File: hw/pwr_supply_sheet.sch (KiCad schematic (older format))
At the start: 11 parts

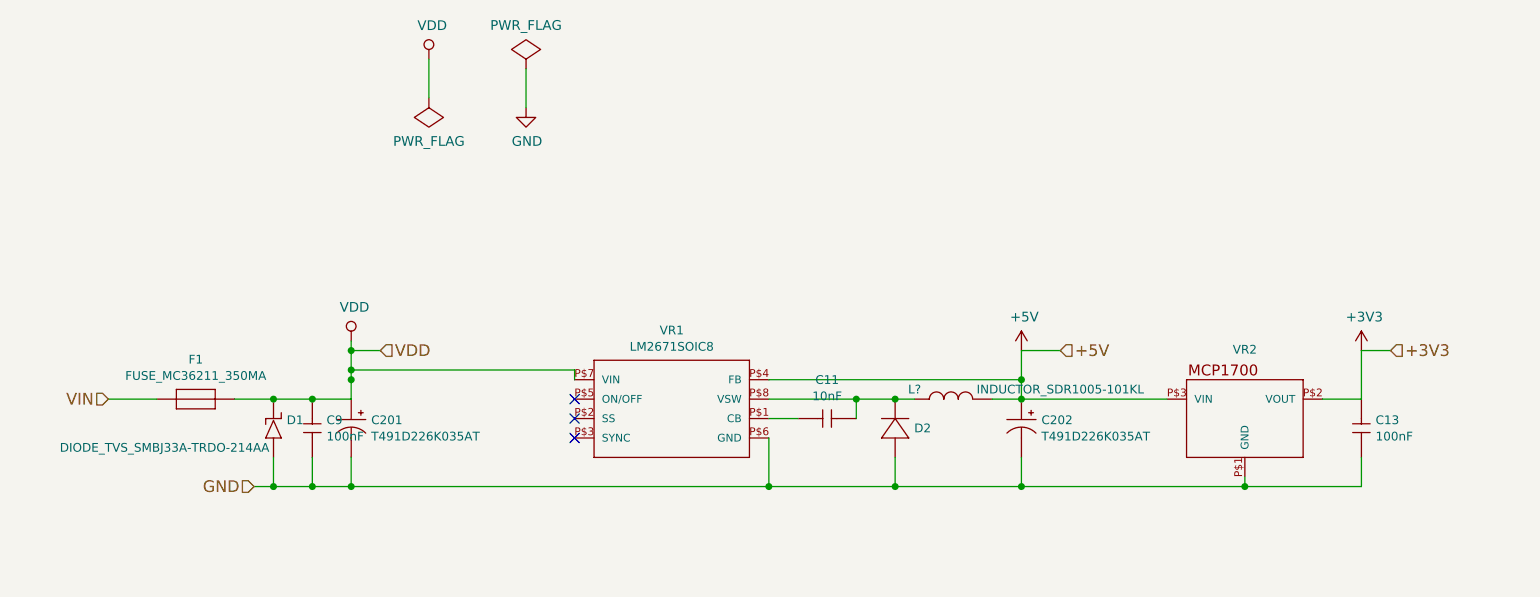
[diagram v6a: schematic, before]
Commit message: version control bug: pwr_supply_sheet now has fuse for LCD as in hw 1.5.0
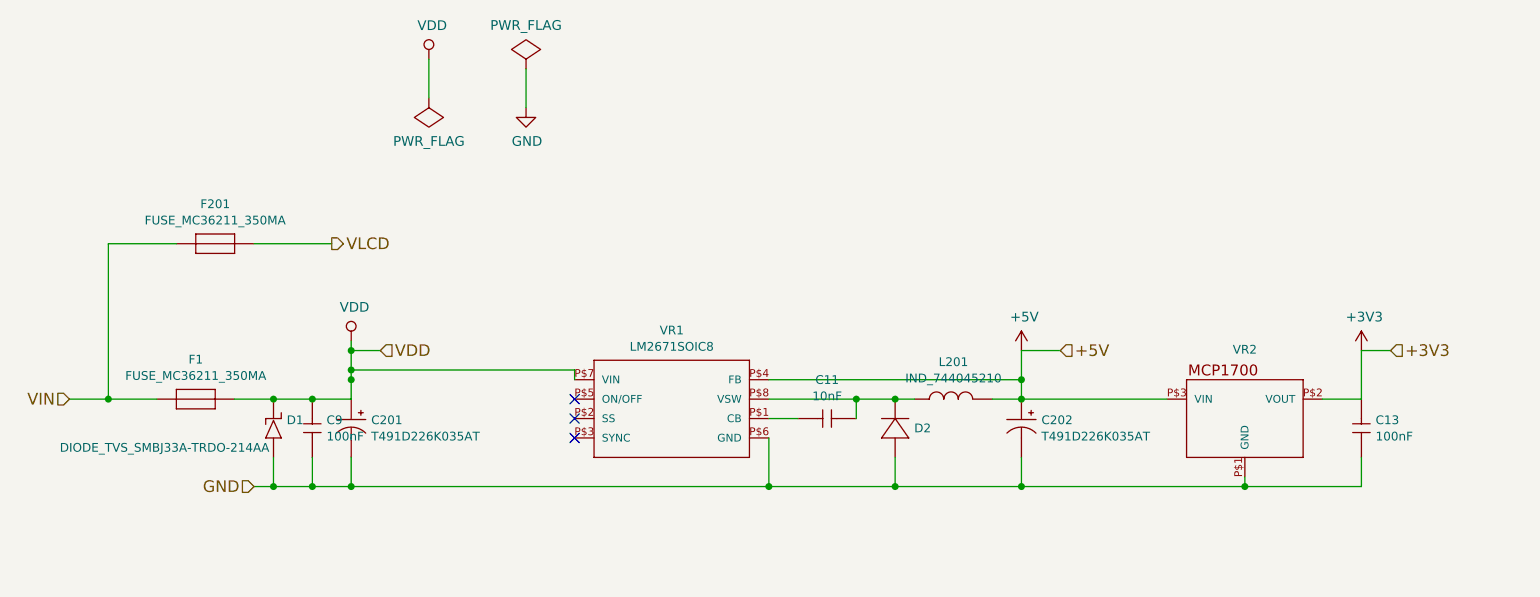
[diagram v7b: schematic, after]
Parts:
- removed L?: INDUCTOR_SDR1005-101KL, usevolt:INDUCTOR_BOURNS_10X13X5MM, symbol INDUCTOR_SDR1005-101KL
- added F201: FUSE_MC36211_350MA, usevolt:FUSE_MC36211, symbol FUSE_MC36211_350MA
- added L201: IND_744045210, usevolt:IND_744045210, symbol IND_744045210
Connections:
- net +5V: now also L201.2
- net VIN: now also F201.P$1
- net at C11.2 (C2), D2.P$2 (N), VR1.P$8 (VSW): now also L201.1
- new net VLCD: F201.P$2
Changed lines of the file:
@@
 Comment4 ""
 $EndDescr
-Text HLabel 2150 3850 0    60   Input ~ 0
+Text HLabel 1950 3850 0    60   Input ~ 0
 VIN
 $Comp
@@
 $EndComp
 Wire Wire Line
-	2400 3850 2150 3850
+	2400 3850 1950 3850
 Wire Wire Line
 	3400 3700 4550 3700
@@
 	4300 2150 4300 2350
 Wire Wire Line
-	8600 4150 8600 4300
-Wire Wire Line
-	8600 4300 2900 4300
+	8600 4300 8600 4150
+Wire Wire Line
+	2900 4300 8600 4300
 $Comp
 L T491D226K035AT C202
@@
 $EndComp
 $Comp
-L INDUCTOR_SDR1005-101KL L?
-U 1 1 58FFA1B5
+L FUSE_MC36211_350MA F201
+U 1 1 594FEE3D
+P 2700 3050
+F 0 "F201" H 2700 3254 45  0000 C CNN
+F 1 "FUSE_MC36211_350MA" H 2700 3170 45  0000 C CNN
+F 2 "usevolt:FUSE_MC36211" H 2730 3200 20  0001 C CNN
+F 3 "http://www.farnell.com/datasheets/1678471.pdf?_ga=1.218604761.1948984246.1460023966" H 2820 3070 60  0001 C CNN
+F 4 "Farnell" H 3120 3370 60  0001 C CNN "1st Source"
+F 5 "MC36211" H 3020 3270 60  0001 C CNN "Manufacturer Part Number"
+F 6 "MC36211" H 3220 3470 60  0001 C CNN "1st Source Part Number"
+F 7 "Multicomp" H 2920 3170 60  0001 C CNN "Manufacturer"
+	1    2700 3050
+	1    0    0    -1
+$EndComp
+Wire Wire Line
+	2150 3850 2150 3050
+Wire Wire Line
+	2150 3050 2500 3050
+Connection ~ 2150 3850
+Wire Wire Line
+	2900 3050 3300 3050
+Text HLabel 3300 3050 2    60   Output ~ 0
+VLCD
+$Comp
+L IND_744045210 L201
+U 1 1 594FF8F5
 P 6500 3850
-F 0 "L?" H 6300 3900 45  0000 C CNN
-F 1 "INDUCTOR_SDR1005-101KL" H 7050 3900 45  0000 C CNN
-F 2 "usevolt:INDUCTOR_BOURNS_10X13X5MM" H 6530 4000 20  0001 C CNN
-F 3 "http://www.farnell.com/datasheets/1695384.pdf?_ga=1.223340891.1948984246.1460023966" H 6400 3790 60  0001 C CNN
-F 4 "1828057" H 6800 4190 60  0001 C CNN "1st Source Part Number"
-F 5 "BOURNS" H 6500 3890 60  0001 C CNN "Manufacturer"
+F 0 "L201" H 6500 4041 45  0000 C CNN
+F 1 "IND_744045210" H 6500 3957 45  0000 C CNN
+F 2 "usevolt:IND_744045210" H 6530 4000 20  0001 C CNN
+F 3 "http://www.farnell.com/datasheets/1735442.pdf?_ga=1.223184091.1948984246.1460023966" H 6400 3790 60  0001 C CNN
+F 4 "1800416" H 6800 4190 60  0001 C CNN "1st Source Part Number"
+F 5 "WURTH ELEKTRONIK" H 6500 3890 60  0001 C CNN "Manufacturer"
 F 6 "Digi-Key" H 6900 4290 60  0001 C CNN "2nd Source"
 F 7 "Farnell" H 6700 4090 60  0001 C CNN "1st Source"
-F 8 "SDR1005-101KL" H 6600 3990 60  0001 C CNN "Manufacturer Part Number"
-F 9 "SDR1005-101KLCT-ND" H 7000 4390 60  0001 C CNN "2nd Source Part Number"
+F 8 "744045210" H 6600 3990 60  0001 C CNN "Manufacturer Part Number"
+F 9 "732-3072-1-ND" H 7000 4390 60  0001 C CNN "2nd Source Part Number"
 	1    6500 3850
 	1    0    0    -1

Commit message: implementing a multilinguality
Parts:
- VR1: symbol LM2671SOIC8 -> LM2671SOIC8-RESCUE-display
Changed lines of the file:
@@
 $EndComp
 $Comp
-L LM2671SOIC8 VR1
+L LM2671SOIC8-RESCUE-display VR1
 U 1 1 57B82261
 P 4850 4150
+AR Path="/57B82261" Ref="VR1"  Part="1"
+AR Path="/57B81D4F/57B82261" Ref="VR1"  Part="1"
 F 0 "VR1" H 5050 4804 45  0000 C CNN
 F 1 "LM2671SOIC8" H 5050 4720 45  0000 C CNN
